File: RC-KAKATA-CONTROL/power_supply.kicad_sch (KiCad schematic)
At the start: 49 parts, among them J3 Screw_Terminal_01x02, J4 Screw_Terminal_01x02, U1 PS-TO220, U2 PS-TO220

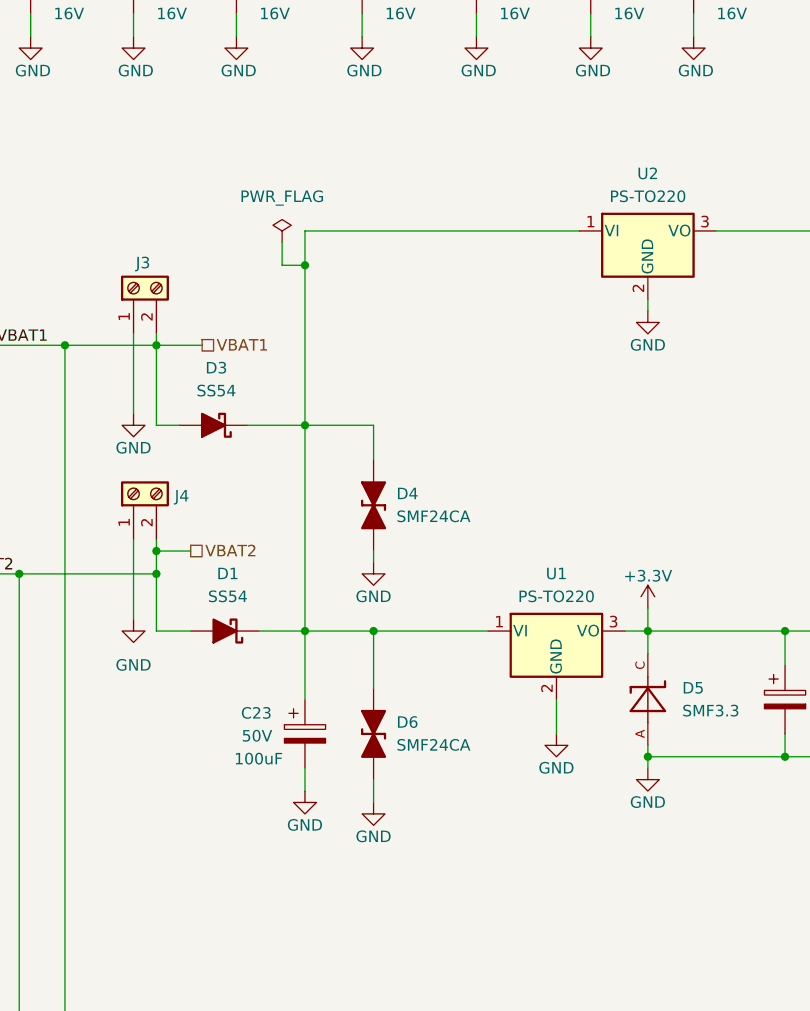
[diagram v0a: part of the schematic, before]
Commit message: Creadas Conexiones de GND y +3.3V Creada Conexion de +5 Creadas las conexiones criticas de Flash - SPI - I2C
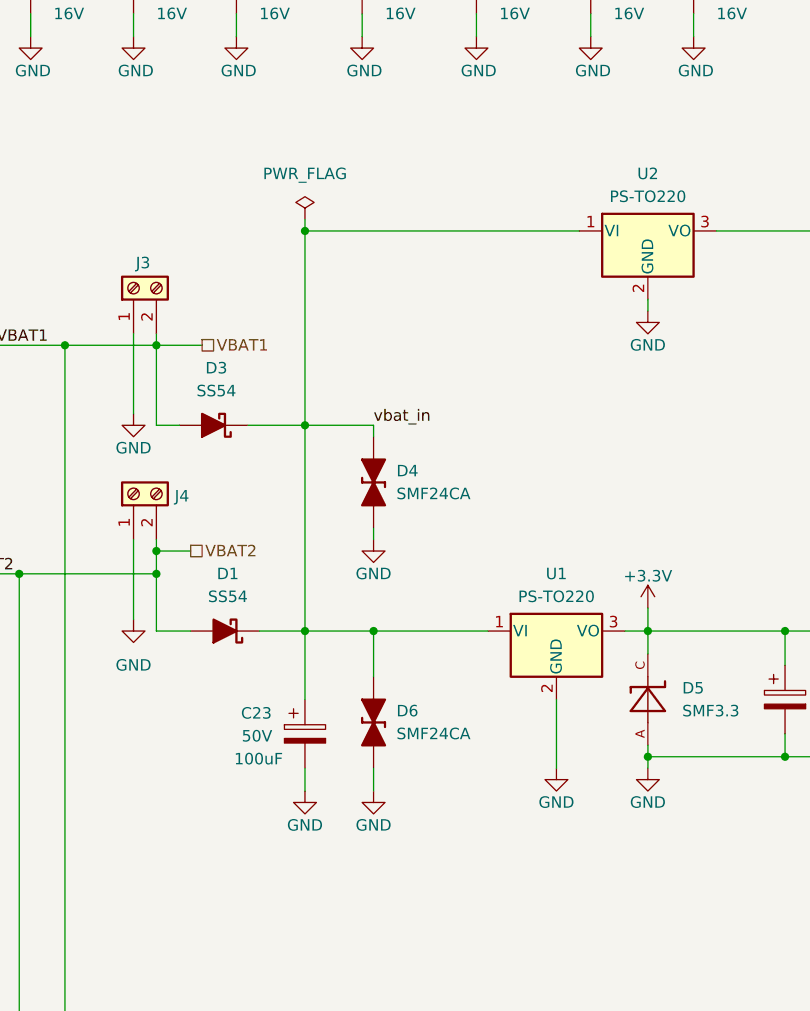
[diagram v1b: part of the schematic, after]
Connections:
- net vbat_in: now reaches C23.1, D1.1 (K), D3.1 (K), D4.2 (A), D6.2 (A), U1.1 (VI), U2.1 (VI)
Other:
- moved on the sheet: D4, D6
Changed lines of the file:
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@@
 	)
 	(junction
+		(at 60.96 48.26)
+		(diameter 0)
+		(color 0 0 0 0)
+	)
+	(junction
 		(at 185.42 78.74)
 		(diameter 0)
@@
 	)
 	(junction
-		(at 60.96 52.07)
-		(diameter 0)
-		(color 0 0 0 0)
-	)
-	(junction
 		(at 77.47 147.32)
 		(diameter 0)
@@
 	(wire
 		(pts
-			(xy 60.96 48.26) (xy 60.96 52.07)
-		)
-		(stroke
-			(width 0)
-			(type default)
-		)
-	)
-	(wire
-		(pts
 			(xy 41.91 82.55) (xy 41.91 91.44)
 		)
@@
 	(wire
 		(pts
-			(xy 58.42 52.07) (xy 60.96 52.07)
-		)
-		(stroke
-			(width 0)
-			(type default)
-		)
-	)
-	(wire
-		(pts
 			(xy 99.06 55.88) (xy 99.06 57.15)
 		)
@@
 	(wire
 		(pts
-			(xy 68.58 92.71) (xy 68.58 99.06)
+			(xy 68.58 92.71) (xy 68.58 97.79)
 		)
 		(stroke
@@
 	(wire
 		(pts
-			(xy 68.58 73.66) (xy 68.58 69.85)
+			(xy 68.58 71.12) (xy 68.58 69.85)
 		)
 		(stroke
@@
 	(wire
 		(pts
-			(xy 68.58 83.82) (xy 68.58 85.09)
+			(xy 68.58 81.28) (xy 68.58 82.55)
 		)
 		(stroke
@@
 	(wire
 		(pts
-			(xy 68.58 109.22) (xy 68.58 111.76)
+			(xy 68.58 107.95) (xy 68.58 110.49)
 		)
 		(stroke
@@
 	(wire
 		(pts
-			(xy 58.42 49.53) (xy 58.42 52.07)
+			(xy 60.96 46.99) (xy 60.96 48.26)
 		)
 		(stroke
@@
 	(wire
 		(pts
-			(xy 60.96 52.07) (xy 60.96 69.85)
+			(xy 60.96 48.26) (xy 60.96 69.85)
 		)
 		(stroke
@@
 	(wire
 		(pts
-			(xy 88.9 100.33) (xy 88.9 104.14)
+			(xy 88.9 100.33) (xy 88.9 107.95)
 		)
 		(stroke
@@
 		)
 	)
+	(label "vbat_in"
+		(at 68.58 69.85 0)
+		(effects
+			(font
+				(size 1.27 1.27)
+			)
+			(justify left bottom)
+		)
+	)
 	(hierarchical_label "VBAT1"
 		(shape passive)
@@
 	(symbol
 		(lib_id "Diode_TVS_AKL:SMF24CA")
-		(at 68.58 104.14 90)
+		(at 68.58 102.87 90)
 		(unit 1)
 		(exclude_from_sim no)
@@
 		(fields_autoplaced yes)
 		(property "Reference" "D6"
-			(at 71.12 102.8699 90)
+			(at 71.12 101.5999 90)
 			(effects
 				(font
@@
 		)
 		(property "Value" "SMF24CA"
-			(at 71.12 105.4099 90)
+			(at 71.12 104.1399 90)
 			(effects
 				(font
@@
 		)
 		(property "Footprint" "Diode_SMD_AKL:D_SOD-123F"
-			(at 68.58 104.14 0)
+			(at 68.58 102.87 0)
 			(effects
 				(font
@@
 		)
 		(property "Datasheet" "https://www.tme.eu/Document/95faf1e5e821ed1b438500c66c7b0bd9/smf50a.pdf"
-			(at 68.58 104.14 0)
+			(at 68.58 102.87 0)
 			(effects
 				(font
@@
 		)
 		(property "Description" "SOD-123F Bidirectional TVS Diode, 24V, 200W, Alternate KiCAD Library"
-			(at 68.58 104.14 0)
+			(at 68.58 102.87 0)
 			(effects
 				(font
@@
 	(symbol
 		(lib_id "power:GND")
-		(at 68.58 111.76 0)
+		(at 68.58 110.49 0)
 		(unit 1)
 		(exclude_from_sim no)
@@
 		(dnp no)
 		(property "Reference" "#PWR37"
-			(at 68.58 118.11 0)
+			(at 68.58 116.84 0)
 			(effects
 				(font
@@
 		)
 		(property "Value" "GND"
-			(at 68.58 115.57 0)
+			(at 68.58 114.3 0)
 			(effects
 				(font
@@
 		)
 		(property "Footprint" ""
-			(at 68.58 111.76 0)
+			(at 68.58 110.49 0)
 			(effects
 				(font
@@
 		)
 		(property "Datasheet" ""
-			(at 68.58 111.76 0)
+			(at 68.58 110.49 0)
 			(effects
 				(font
@@
 		)
 		(property "Description" "Power symbol creates a global label with name \"GND\" , ground"
-			(at 68.58 111.76 0)
+			(at 68.58 110.49 0)
 			(effects
 				(font
@@
 	(symbol
 		(lib_id "Diode_TVS_AKL:SMF24CA")
-		(at 68.58 78.74 90)
+		(at 68.58 76.2 90)
 		(unit 1)
 		(exclude_from_sim no)
@@
 		(fields_autoplaced yes)
 		(property "Reference" "D4"
-			(at 71.12 77.4699 90)
+			(at 71.12 74.9299 90)
 			(effects
 				(font
@@
 		)
 		(property "Value" "SMF24CA"
-			(at 71.12 80.0099 90)
+			(at 71.12 77.4699 90)
 			(effects
 				(font
@@
 		)
 		(property "Footprint" "Diode_SMD_AKL:D_SOD-123F"
-			(at 68.58 78.74 0)
+			(at 68.58 76.2 0)
 			(effects
 				(font
@@
 		)
 		(property "Datasheet" "https://www.tme.eu/Document/95faf1e5e821ed1b438500c66c7b0bd9/smf50a.pdf"
-			(at 68.58 78.74 0)
+			(at 68.58 76.2 0)
 			(effects
 				(font
@@
 		)
 		(property "Description" "SOD-123F Bidirectional TVS Diode, 24V, 200W, Alternate KiCAD Library"
-			(at 68.58 78.74 0)
+			(at 68.58 76.2 0)
 			(effects
 				(font
@@
 	(symbol
 		(lib_id "power:GND")
-		(at 88.9 104.14 0)
+		(at 88.9 107.95 0)
 		(unit 1)
 		(exclude_from_sim no)
@@
 		(dnp no)
 		(property "Reference" "#PWR33"
-			(at 88.9 110.49 0)
+			(at 88.9 114.3 0)
 			(effects
 				(font
@@
 		)
 		(property "Value" "GND"
-			(at 88.9 107.95 0)
+			(at 88.9 111.76 0)
 			(effects
 				(font
@@
 		)
 		(property "Footprint" ""
-			(at 88.9 104.14 0)
+			(at 88.9 107.95 0)
 			(effects
 				(font
@@
 		)
 		(property "Datasheet" ""
-			(at 88.9 104.14 0)
+			(at 88.9 107.95 0)
 			(effects
 				(font
@@
 		)
 		(property "Description" "Power symbol creates a global label with name \"GND\" , ground"
-			(at 88.9 104.14 0)
+			(at 88.9 107.95 0)
 			(effects
 				(font
@@
 	(symbol
 		(lib_id "power:PWR_FLAG")
-		(at 58.42 49.53 0)
+		(at 60.96 46.99 0)
 		(unit 1)
 		(exclude_from_sim no)
@@
 		(fields_autoplaced yes)
 		(property "Reference" "#FLG01"
-			(at 58.42 47.625 0)
+			(at 60.96 45.085 0)
 			(effects
 				(font
@@
 		)
 		(property "Value" "PWR_FLAG"
-			(at 58.42 44.45 0)
+			(at 60.96 41.91 0)
 			(effects
 				(font
@@
 		)
 		(property "Footprint" ""
-			(at 58.42 49.53 0)
+			(at 60.96 46.99 0)
 			(effects
 				(font
@@
 		)
 		(property "Datasheet" "~"
-			(at 58.42 49.53 0)
+			(at 60.96 46.99 0)
 			(effects
 				(font
@@
 		)
 		(property "Description" "Special symbol for telling ERC where power comes from"
-			(at 58.42 49.53 0)
+			(at 60.96 46.99 0)
 			(effects
 				(font
@@
 	(symbol
 		(lib_id "power:GND")
-		(at 68.58 85.09 0)
+		(at 68.58 82.55 0)
 		(unit 1)
 		(exclude_from_sim no)
@@
 		(dnp no)
 		(property "Reference" "#PWR0114"
-			(at 68.58 91.44 0)
+			(at 68.58 88.9 0)
 			(effects
 				(font
@@
 		)
 		(property "Value" "GND"
-			(at 68.58 88.9 0)
+			(at 68.58 86.36 0)
 			(effects
 				(font
@@
 		)
 		(property "Footprint" ""
-			(at 68.58 85.09 0)
+			(at 68.58 82.55 0)
 			(effects
 				(font
@@
 		)
 		(property "Datasheet" ""
-			(at 68.58 85.09 0)
+			(at 68.58 82.55 0)
 			(effects
 				(font
@@
 		)
 		(property "Description" "Power symbol creates a global label with name \"GND\" , ground"
-			(at 68.58 85.09 0)
+			(at 68.58 82.55 0)
 			(effects
 				(font

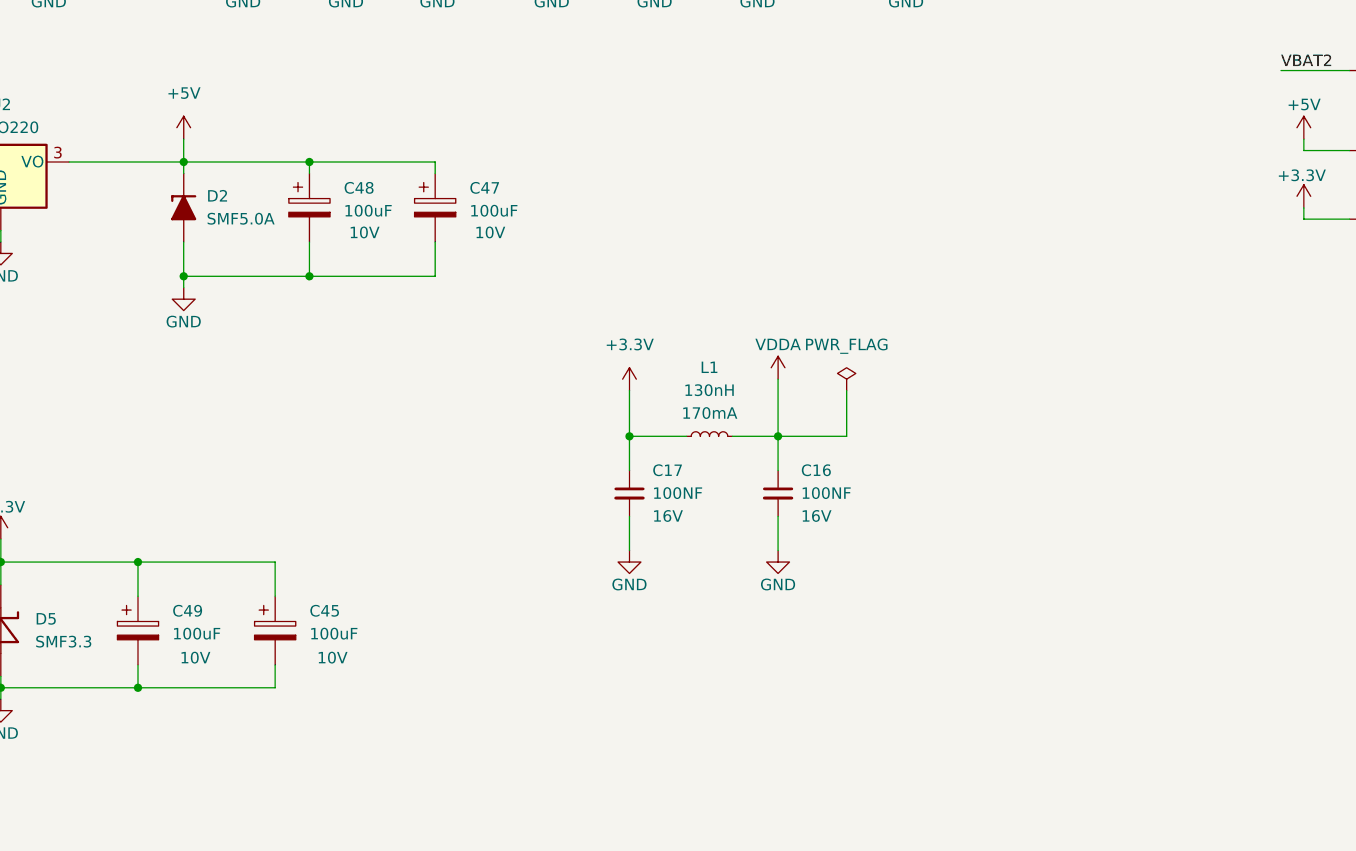
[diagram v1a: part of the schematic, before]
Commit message: Restan 32 pistas por rutear Colocados los Ref de los compoentes
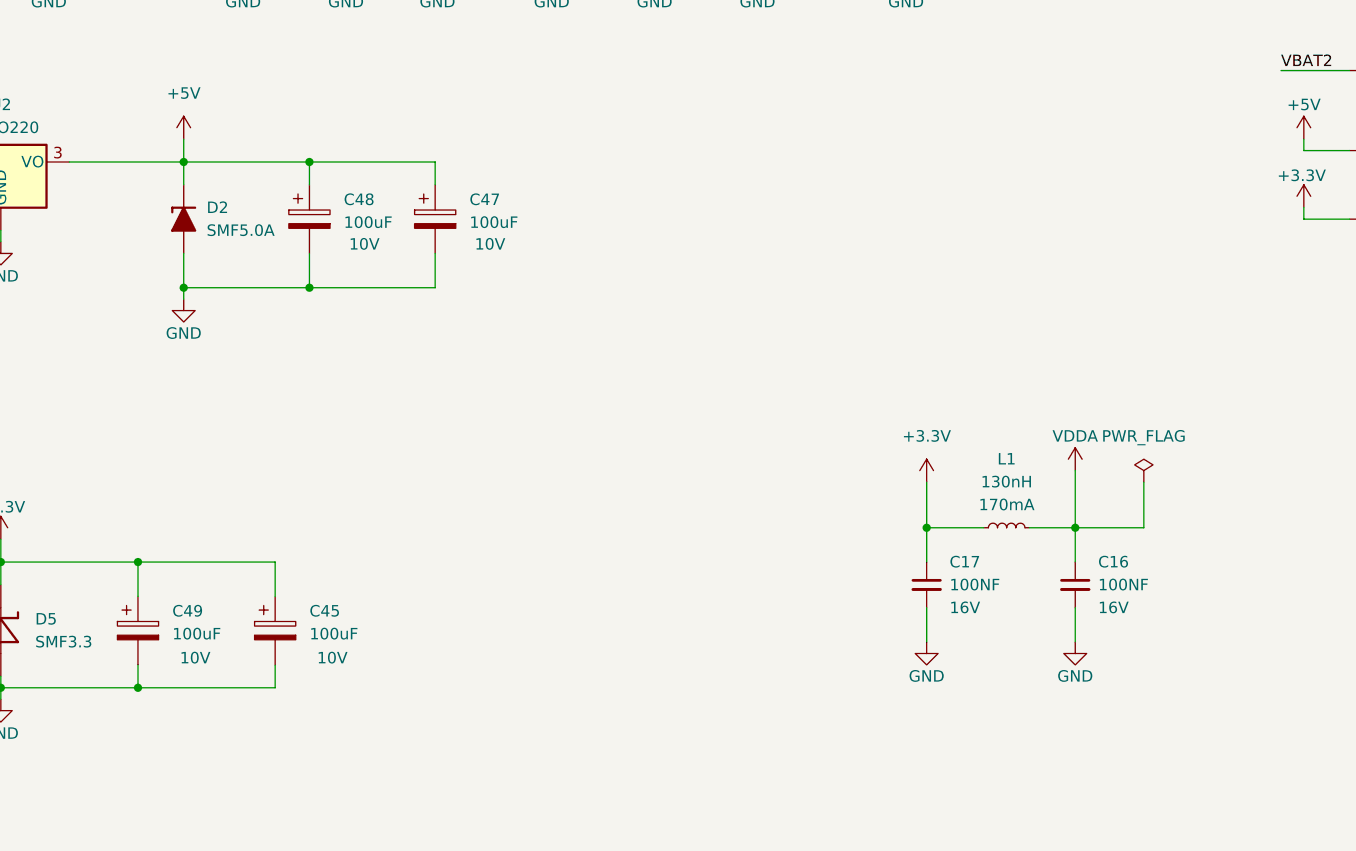
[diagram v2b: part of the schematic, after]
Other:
- moved on the sheet: C16, C17, C47, C48, D2, L1

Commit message: Completado el BOM
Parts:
- C1, C10, C11, C12, C13, C14, C16, C17, C18, C2, C21, C25, C3, C4, C5, C6, C7, C8, C9: LCSC Part (none) -> C14663
- C20, C22: LCSC Part (none) -> C559769
- C23: LCSC Part (none) -> C116241
- C45, C47, C48, C49: LCSC Part (none) -> C72478
- D1, D3: LCSC Part (none) -> C22452
- D2: LCSC Part (none) -> C151296
- D4, D6: LCSC Part (none) -> C3720035
- D5: LCSC Part (none) -> C6165153
- J3, J4: LCSC Part (none) -> C2915639
- L1: LCSC Part (none) -> C701178
- LED1, LED2, LED3, LED4: LCSC Part (none) -> C965799
- R10, R9: LCSC Part (none) -> C114662
- R11, R6, R8: LCSC Part (none) -> C22548
- R12: LCSC Part (none) -> C114617
- R5, R7: LCSC Part (none) -> C98220
- U1, U2: now not fitted
